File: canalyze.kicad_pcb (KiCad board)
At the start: 2 copper layers, 68 x 31 mm, 40 parts, among them J1 DB9, P1 SWD, P2 USB_B, SW1 SW_PUSH, SW2 SW_PUSH, SW3 SW_DIP_x08, U1 MCP2551-I/SN, U2 STM32F042C6Tx, U3 MCP1700T-3002E/TT, Y1 Crystal

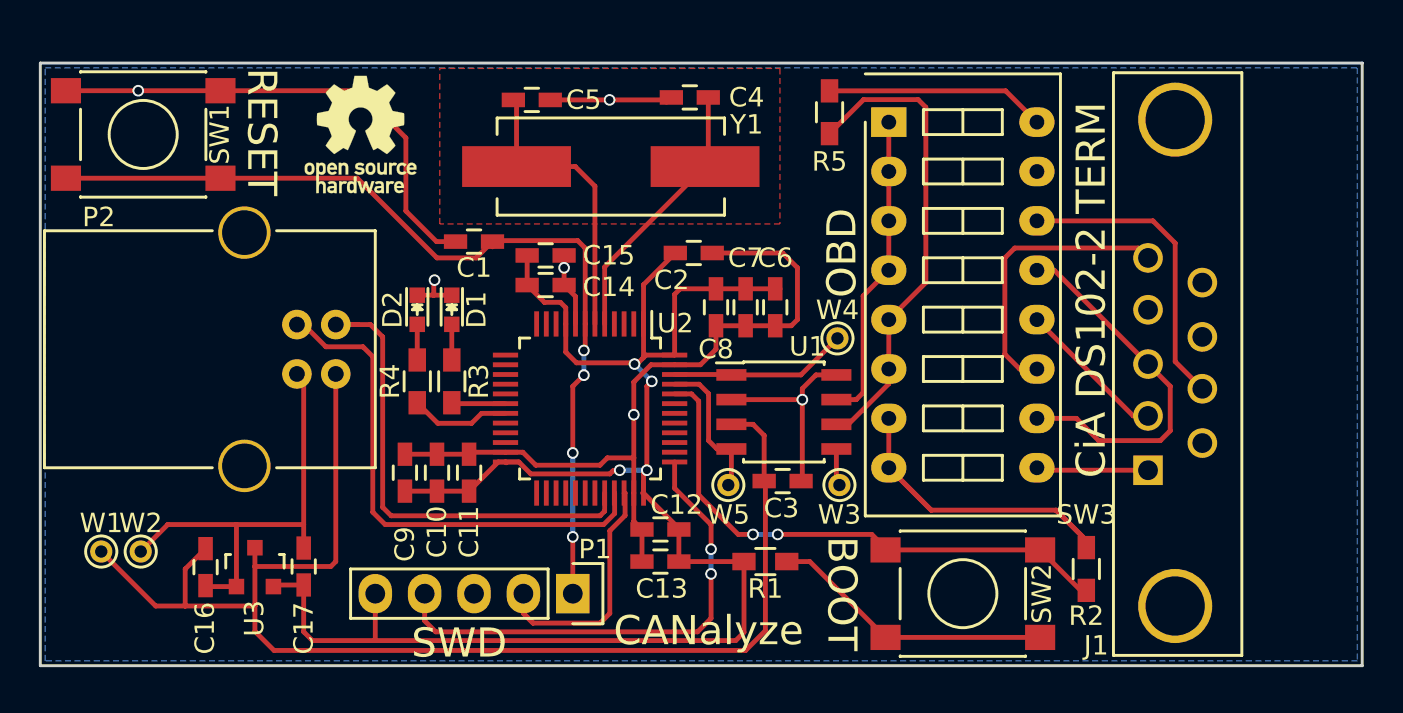
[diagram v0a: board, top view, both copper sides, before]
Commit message: Update to SMD 0805, changed README with TODO
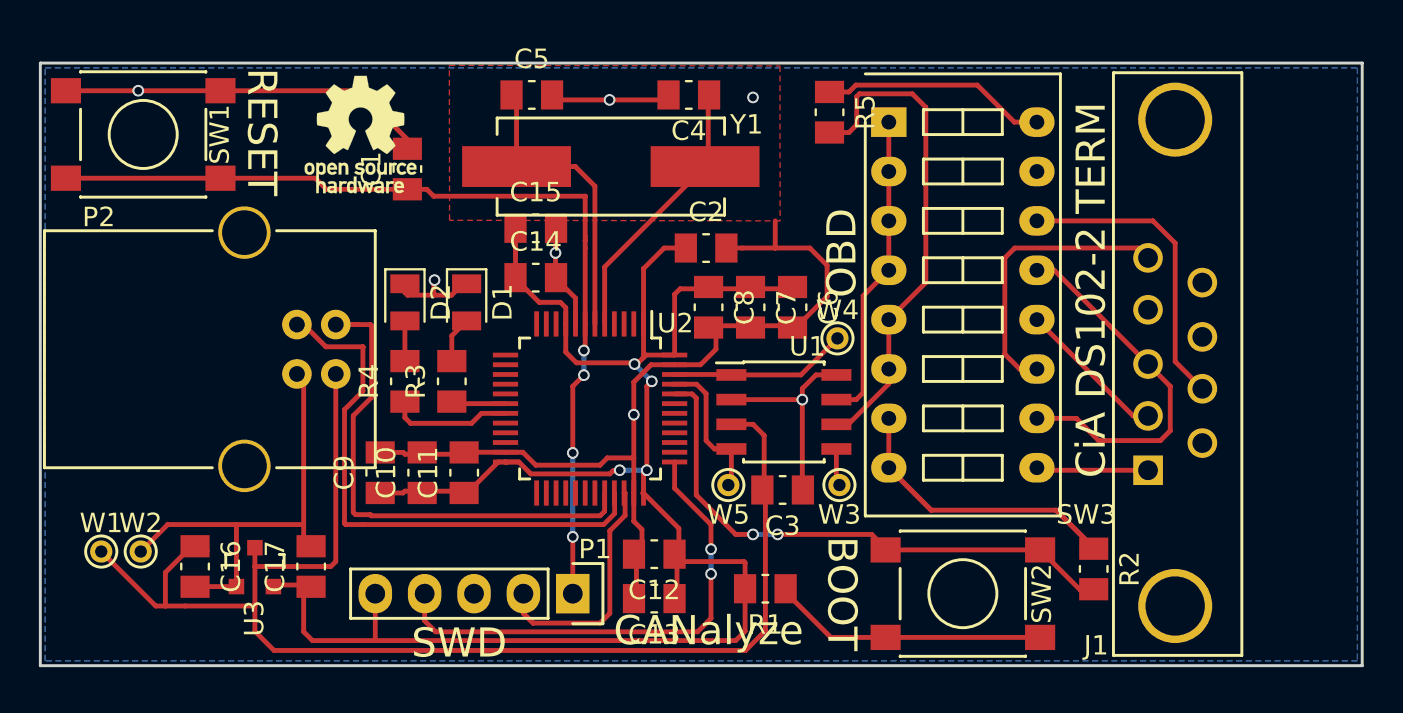
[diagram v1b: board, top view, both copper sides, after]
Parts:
- C1, C10, C11, C12, C13, C14, C15, C16, C17, C2, C3, C4, C5, C6, C7, C8, C9: footprint Capacitors_SMD:C_0603_HandSoldering -> Capacitor_SMD:C_0805_2012Metric_Pad1.15x1.50mm_HandSolder
- D1, D2: footprint LEDs:LED_0603 -> LED_SMD:LED_0805_2012Metric_Pad0.97x1.50mm_HandSolder
- R1, R2, R3, R4, R5: footprint Resistors_SMD:R_0603_HandSoldering -> Resistor_SMD:R_0805_2012Metric_Pad1.15x1.50mm_HandSolder
- moved C1 5.07 mm to (63.9, 52.5), turned to 90 degrees
- moved C13 1.93 mm to (76.6, 74.5)
- moved C15 1.49 mm to (70.5, 55.5)
- moved R1 1.40 mm to (82.3, 74.0)
- moved C12 1.31 mm to (76.6, 72.3)
- moved C9 1.27 mm to (62.5, 68.1)
- moved C6 0.89 mm to (83.7, 59.6)
- moved D1 0.85 mm to (66.9, 59.3)
- moved C10 0.76 mm to (64.6, 68.1)
- moved D2 0.74 mm to (63.8, 59.3)
- moved C2 0.68 mm to (79.2, 56.5)
- moved R4 0.63 mm to (63.8, 63.4)
- moved C14 0.63 mm to (70.5, 58.0)
- moved C16 0.54 mm to (53.0, 72.9)
- moved C3 0.46 mm to (83.2, 69.0)
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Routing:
- net +3V3: track 89.3 -> 96.3 mm
- net GND: track 132.3 -> 137.3 mm, vias 6 -> 7
- net /USB_DP: track 26.9 -> 28.9 mm
- net /USB_DM: track 24.7 -> 26.5 mm
- net Net-(R4-Pad1): track 5.19 -> 6.33 mm
- net /CAN_L: track 24.8 -> 25.9 mm
- net /CAN_RX: track 8.39 -> 9.26 mm
- net Net-(D1-Pad2): track 1.88 -> 2.43 mm
